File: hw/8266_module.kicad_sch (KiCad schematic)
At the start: 5 parts

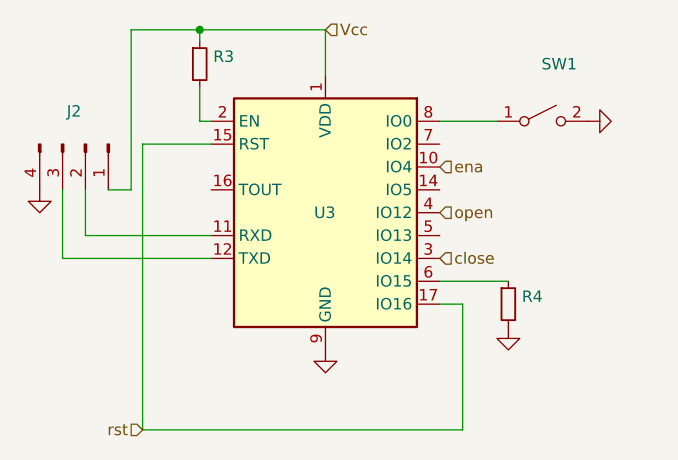
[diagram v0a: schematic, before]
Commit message: Update schematic to include new H bridge
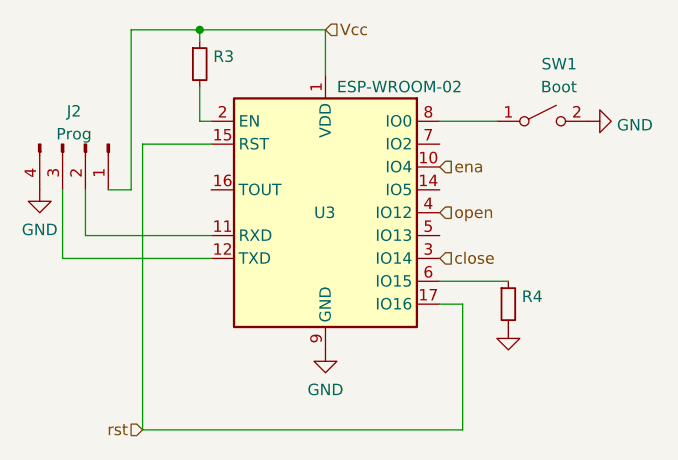
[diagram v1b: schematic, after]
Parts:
- J2: value (none) -> Prog
- R3, R4: value (none) -> ~
- SW1: value (none) -> Boot
- U3: value (none) -> ESP-WROOM-02; footprint (none) -> RF_Module:ESP-WROOM-02
